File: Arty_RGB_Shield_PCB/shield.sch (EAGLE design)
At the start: 23 parts, among them IC1 SN74ALVC164245, IC2 SN74ALVC164245, IC3 TXS0104EPWR

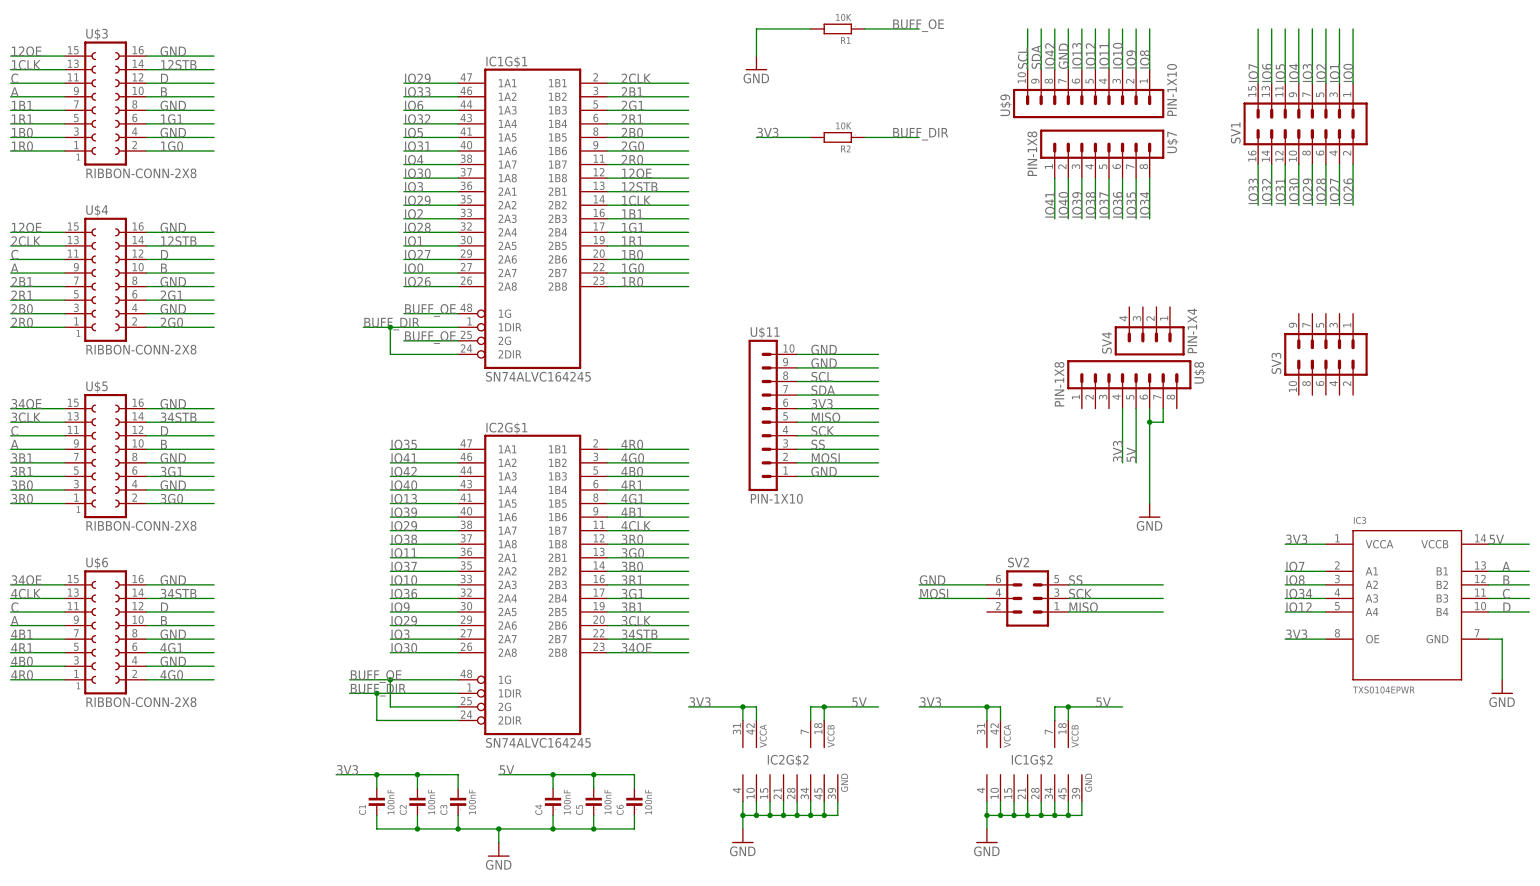
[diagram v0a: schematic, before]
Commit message: add V2 board
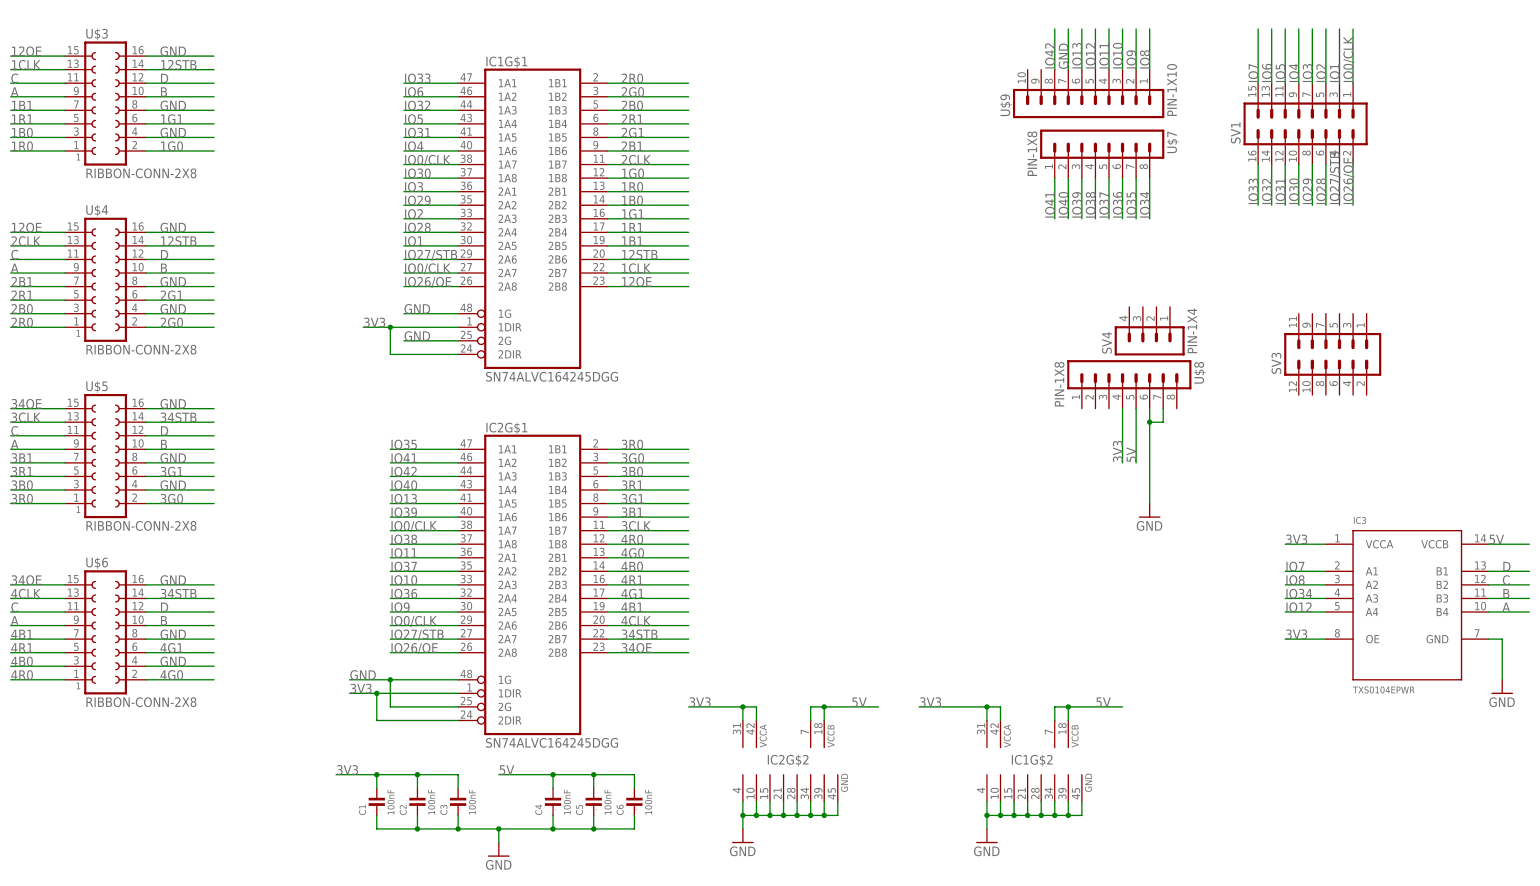
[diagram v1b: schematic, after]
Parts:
- removed R1, R2: 10K, GadgetFactory:R0603
- removed SV2: (no value), con-lstb:MA03-2
- removed U$11: PIN-1X10, alvie:PIN-1X10
- IC1, IC2: value SN74ALVC164245 -> SN74ALVC164245DGG; device alvie:SN74ALVC164245 -> alvie:SN74ALVC164245DGG
- SV3: device con-lstb:MA05-2 -> con-lstb:MA06-2
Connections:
- removed net BUFF_DIR: IC1G$1.1DIR, IC1G$1.2DIR, IC2G$1.1DIR, IC2G$1.2DIR, R2A.1
- removed net BUFF_OE: IC1G$1.1G, IC1G$1.2G, IC2G$1.1G, IC2G$1.2G, R1A.1
- removed net IO0: IC1G$1.2A7, SV1.1
- removed net IO26: IC1G$1.2A8, SV1.2
- removed net IO27: IC1G$1.2A6, SV1.4
- removed net MISO: SV2.1, U$11.5
- removed net MOSI: SV2.4, U$11.2
- removed net SCK: SV2.3, U$11.4
- removed net SCL: U$11.8, U$9.10
- removed net SDA: U$11.7, U$9.9
- removed net SS: SV2.5, U$11.3
- new net IO0/CLK: IC1G$1.1A7, IC1G$1.2A7, IC2G$1.1A7, IC2G$1.2A6, SV1.1
- new net IO26/OE: IC1G$1.2A8, IC2G$1.2A8, SV1.2
- new net IO27/STB: IC1G$1.2A6, IC2G$1.2A7, SV1.4
- net 12OE: now also IC1G$1.2B8; no longer IC1G$1.1B8
- net 12STB: now also IC1G$1.2B6; no longer IC1G$1.2B1
- net 1B0: now also IC1G$1.2B2; no longer IC1G$1.2B6
- net 1B1: now also IC1G$1.2B5; no longer IC1G$1.2B3
- net 1CLK: now also IC1G$1.2B7; no longer IC1G$1.2B2
- net 1G0: now also IC1G$1.1B8; no longer IC1G$1.2B7
- net 1G1: now also IC1G$1.2B3; no longer IC1G$1.2B4
- net 1R0: now also IC1G$1.2B1; no longer IC1G$1.2B8
- net 1R1: now also IC1G$1.2B4; no longer IC1G$1.2B5
- net 2B0: now also IC1G$1.1B3; no longer IC1G$1.1B5
- net 2B1: now also IC1G$1.1B6; no longer IC1G$1.1B2
- net 2CLK: now also IC1G$1.1B7; no longer IC1G$1.1B1
- net 2G0: now also IC1G$1.1B2; no longer IC1G$1.1B6
- net 2G1: now also IC1G$1.1B5; no longer IC1G$1.1B3
- net 2R0: now also IC1G$1.1B1; no longer IC1G$1.1B7
- net 3B0: now also IC2G$1.1B3; no longer IC2G$1.2B2
- net 3B1: now also IC2G$1.1B6; no longer IC2G$1.2B5
- net 3CLK: now also IC2G$1.1B7; no longer IC2G$1.2B6
- net 3G0: now also IC2G$1.1B2; no longer IC2G$1.2B1
- net 3G1: now also IC2G$1.1B5; no longer IC2G$1.2B4
- net 3R0: now also IC2G$1.1B1; no longer IC2G$1.1B8
- net 3R1: now also IC2G$1.1B4; no longer IC2G$1.2B3
- net 3V3: now also IC1G$1.1DIR, IC1G$1.2DIR, IC2G$1.1DIR, IC2G$1.2DIR; no longer R2A.2, U$11.6
- net 4B0: now also IC2G$1.2B2; no longer IC2G$1.1B3
- net 4B1: now also IC2G$1.2B5; no longer IC2G$1.1B6
- net 4CLK: now also IC2G$1.2B6; no longer IC2G$1.1B7
- net 4G0: now also IC2G$1.2B1; no longer IC2G$1.1B2
- net 4G1: now also IC2G$1.2B4; no longer IC2G$1.1B5
- net 4R0: now also IC2G$1.1B8; no longer IC2G$1.1B1
- net 4R1: now also IC2G$1.2B3; no longer IC2G$1.1B4
- net A: now also IC3.B4; no longer IC3.B1
- net B: now also IC3.B3; no longer IC3.B2
- net C: now also IC3.B2; no longer IC3.B3
- net D: now also IC3.B1; no longer IC3.B4
- net GND: now also IC1G$1.1G, IC1G$1.2G, IC2G$1.1G, IC2G$1.2G; no longer R1A.2, SV2.6, U$11.1, U$11.10, U$11.9
- net IO29: no longer IC1G$1.1A1, IC2G$1.1A7, IC2G$1.2A6
- net IO3: no longer IC2G$1.2A7
- net IO30: no longer IC2G$1.2A8
- net IO31: now also IC1G$1.1A5; no longer IC1G$1.1A6
- net IO32: now also IC1G$1.1A3; no longer IC1G$1.1A4
- net IO33: now also IC1G$1.1A1; no longer IC1G$1.1A2
- net IO4: now also IC1G$1.1A6; no longer IC1G$1.1A7
- net IO5: now also IC1G$1.1A4; no longer IC1G$1.1A5
- net IO6: now also IC1G$1.1A2; no longer IC1G$1.1A3
